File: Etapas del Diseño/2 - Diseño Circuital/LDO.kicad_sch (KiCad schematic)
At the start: 5 parts, among them Q1 2N3904, U1 TL431LP

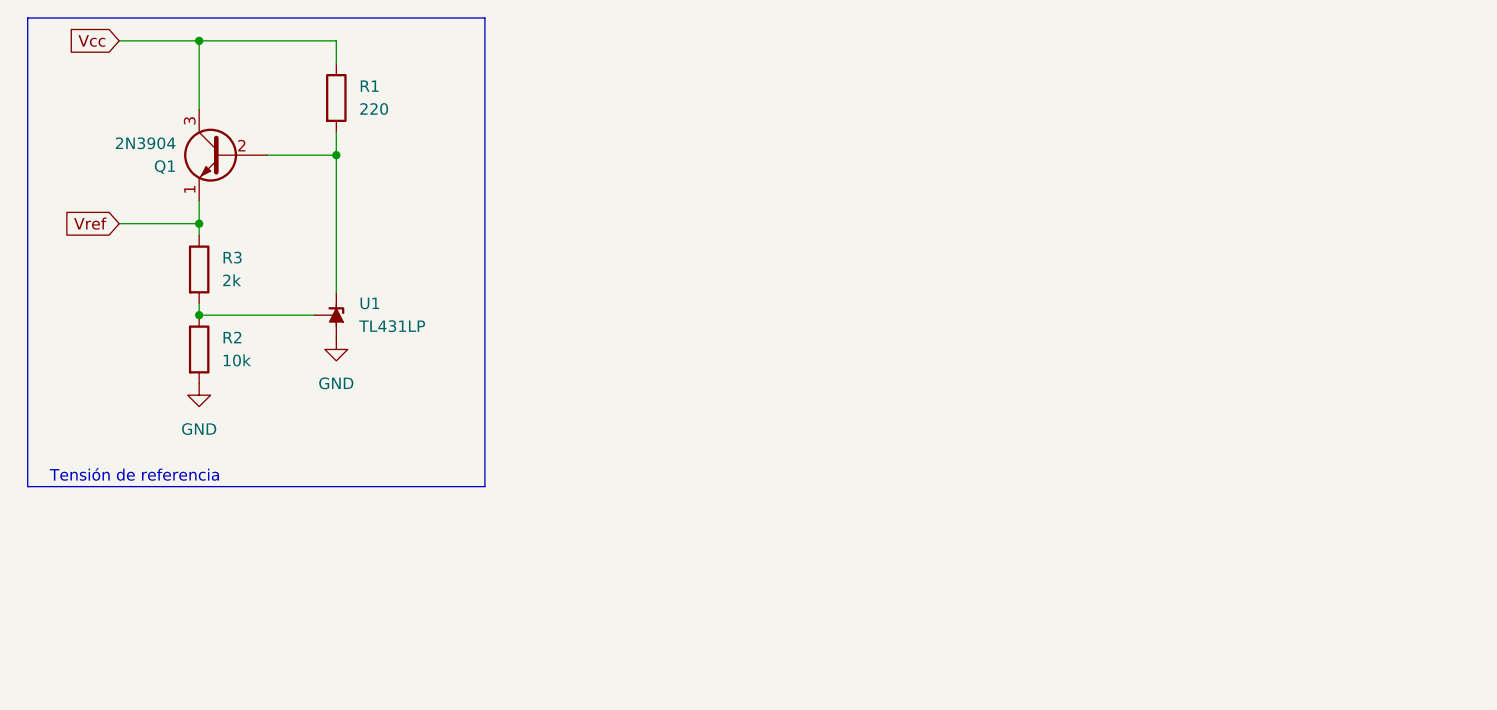
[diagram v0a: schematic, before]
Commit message: Vref y amplificador en esquemtico
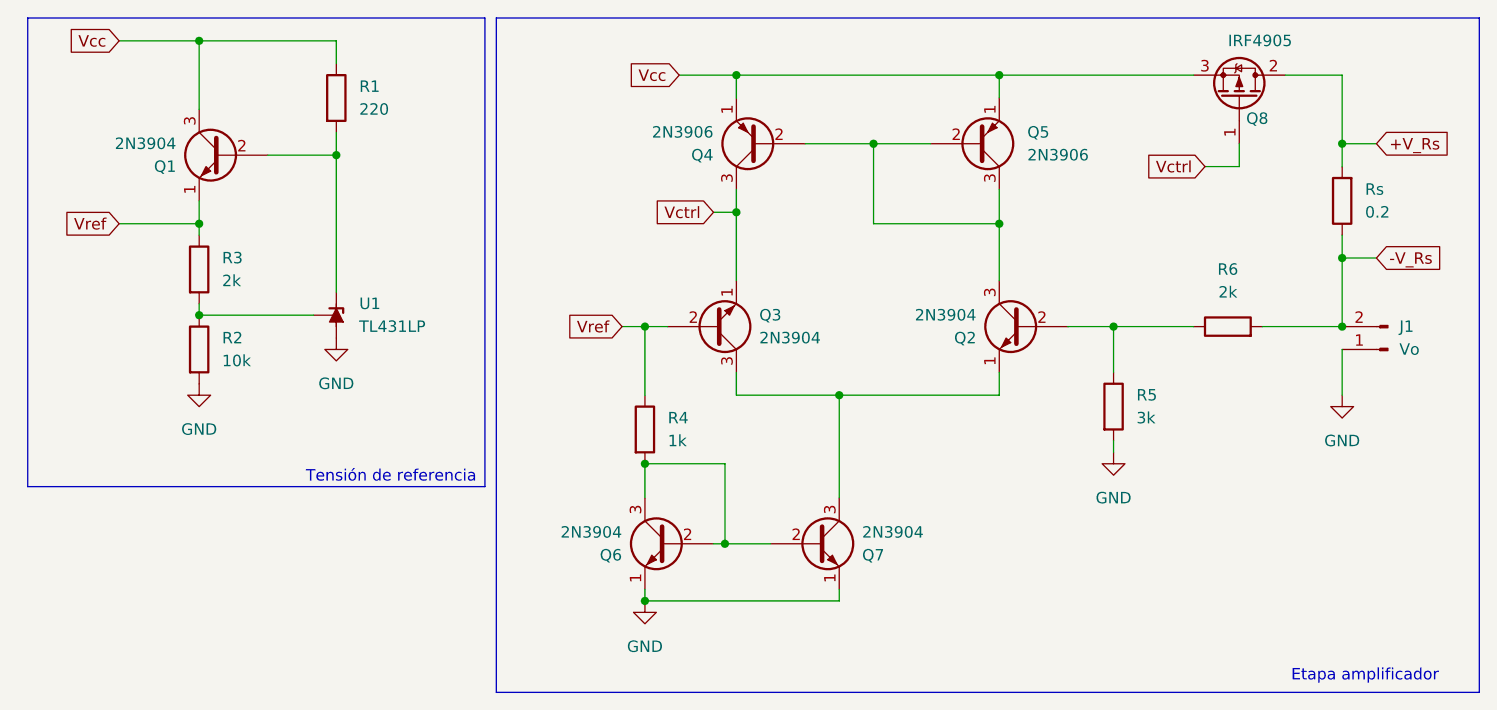
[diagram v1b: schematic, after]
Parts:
- added J1: Vo, symbol Connector:Conn_01x02_Pin
- added Q2, Q3, Q6, Q7: 2N3904, Package_TO_SOT_THT:TO-92_Inline, symbol Transistor_BJT:2N3904
- added Q4, Q5: 2N3906, Package_TO_SOT_THT:TO-92_Inline, symbol Transistor_BJT:2N3906
- added Q8: IRF4905, Package_TO_SOT_THT:TO-220-3_Vertical, symbol Transistor_FET:IRF4905
- added R4: 1k, symbol Device:R
- added R5: 3k, symbol Device:R
- added R6: 2k, symbol Device:R
- added Rs: 0.2, symbol Device:R
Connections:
- net GND: now also J1.1 (Pin_1), Q6.1 (E), Q7.1 (E), R5.2
- net Vcc: now also Q4.1 (E), Q5.1 (E), Q8.3 (S)
- net Vref: now also Q3.2 (B), R4.1
- new net: Q6.2 (B), Q6.3 (C), Q7.2 (B), R4.2
- new net: Q2.1 (E), Q3.3 (C), Q7.3 (C)
- new net: Q2.2 (B), R5.1, R6.1
- new net: Q2.3 (C), Q4.2 (B), Q5.2 (B), Q5.3 (C)
- new net +V_Rs: Q8.2 (D), Rs.2
- new net -V_Rs: J1.2 (Pin_2), R6.2, Rs.1
- new net Vctrl: Q3.1 (E), Q4.3 (C), Q8.1 (G)
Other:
- note added: "Etapa amplificador"

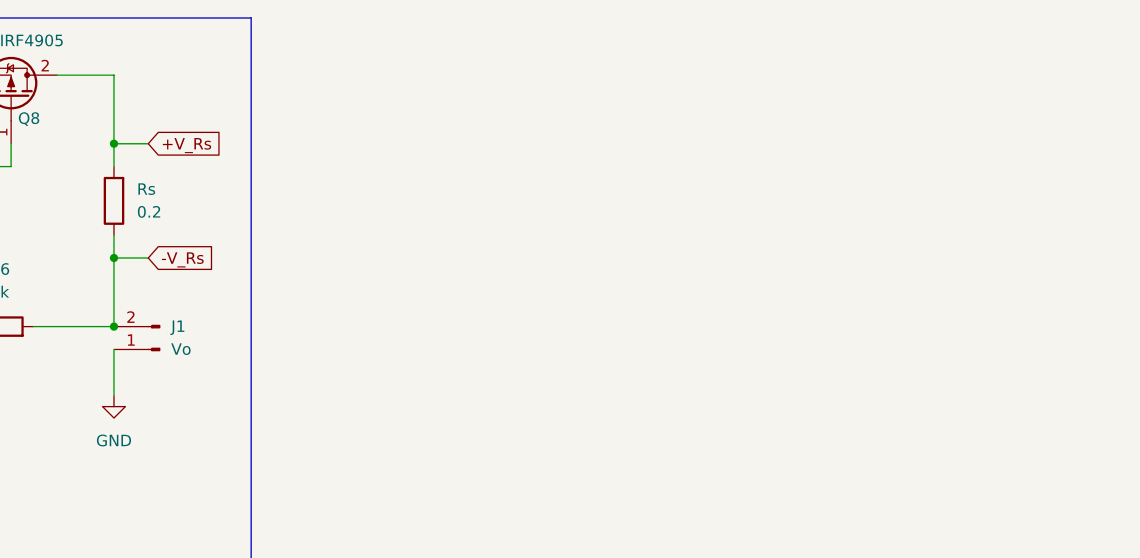
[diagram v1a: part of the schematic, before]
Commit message: Vref y amplificador en esquemtico 2
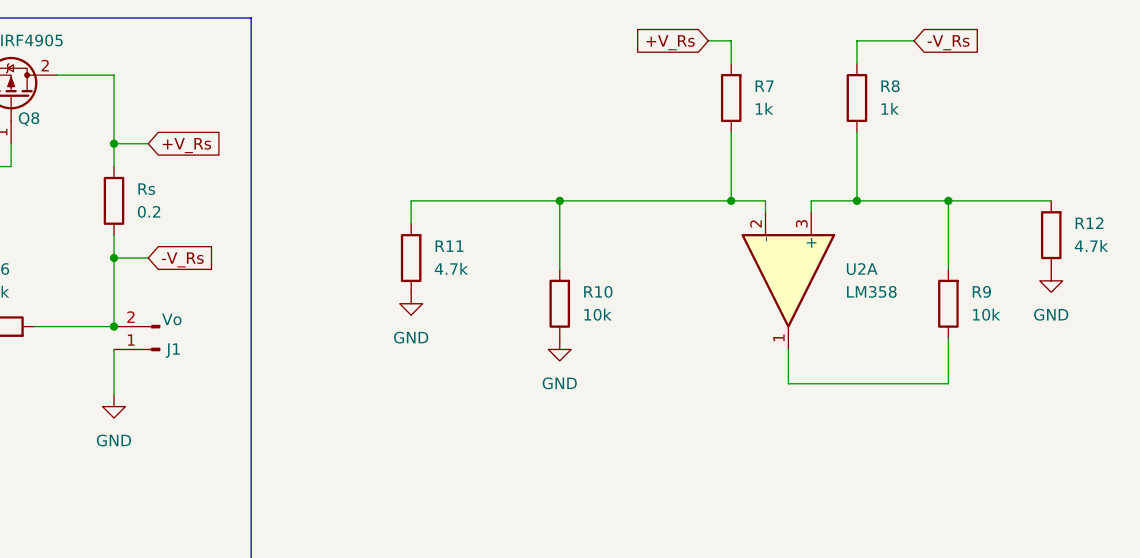
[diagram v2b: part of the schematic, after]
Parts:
- added R10, R9: 10k, symbol Device:R
- added R11, R12: 4.7k, symbol Device:R
- added R7, R8: 1k, symbol Device:R
- added U2: LM358, symbol Amplifier_Operational:LM358
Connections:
- net +V_Rs: now also R7.2
- net -V_Rs: now also R8.2
- net GND: now also R10.1, R11.1, R12.1
- new net: R9.1, U2.1
- new net: R10.2, R11.2, R7.1, U2.2 (-)
- new net: R12.2, R8.1, R9.2, U2.3 (+)

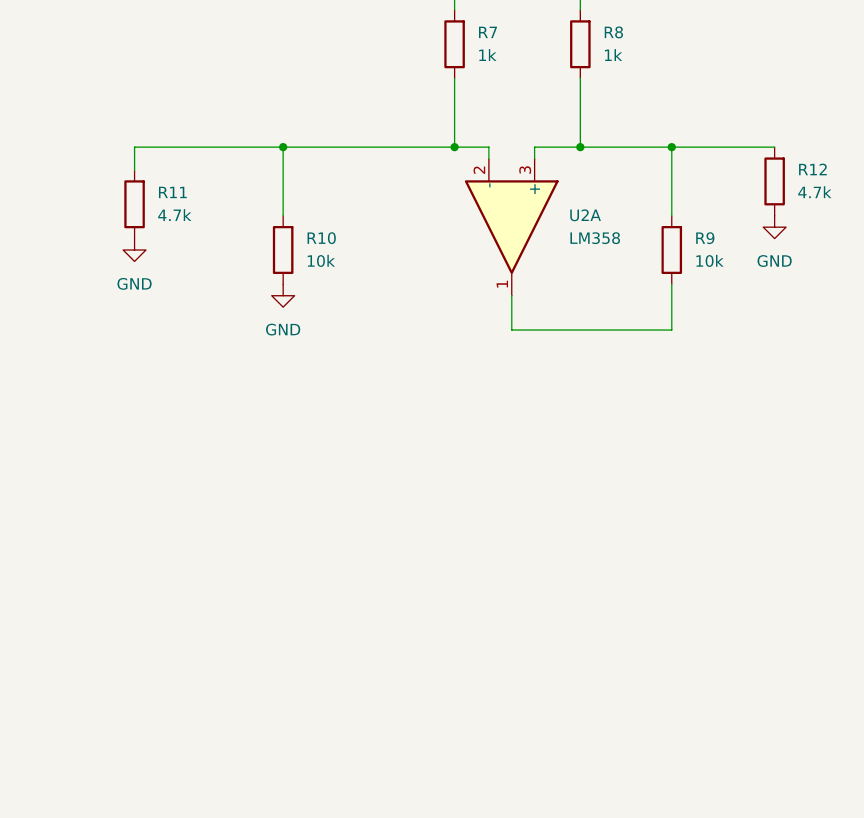
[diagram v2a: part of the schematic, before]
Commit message: Bloque aparte para el lazo de reg de corriente, tome referencias de Rs
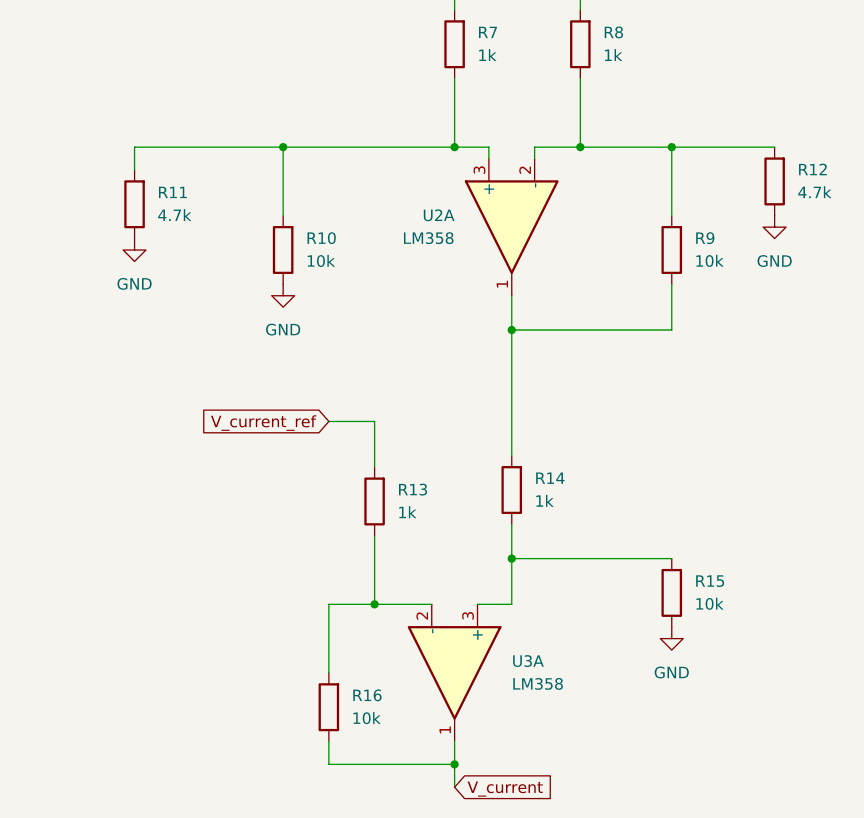
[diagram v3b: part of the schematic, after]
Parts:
- added R13, R14: 1k, symbol Device:R
- added R15, R16: 10k, symbol Device:R
- added U3: LM358, symbol Amplifier_Operational:LM358
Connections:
- net GND: now also R15.1
- net at R9.1, U2.1: now also R14.2
- net at R10.2, R11.2, R7.1: now also U2.3 (+); no longer U2.2 (-)
- net at R12.2, R8.1, R9.2: now also U2.2 (-); no longer U2.3 (+)
- new net: R14.1, R15.2, U3.3 (+)
- new net: R13.1, R16.2, U3.2 (-)
- new net V_current: R16.1, U3.1
- new net V_current_ref: R13.2
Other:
- moved on the sheet: U2A

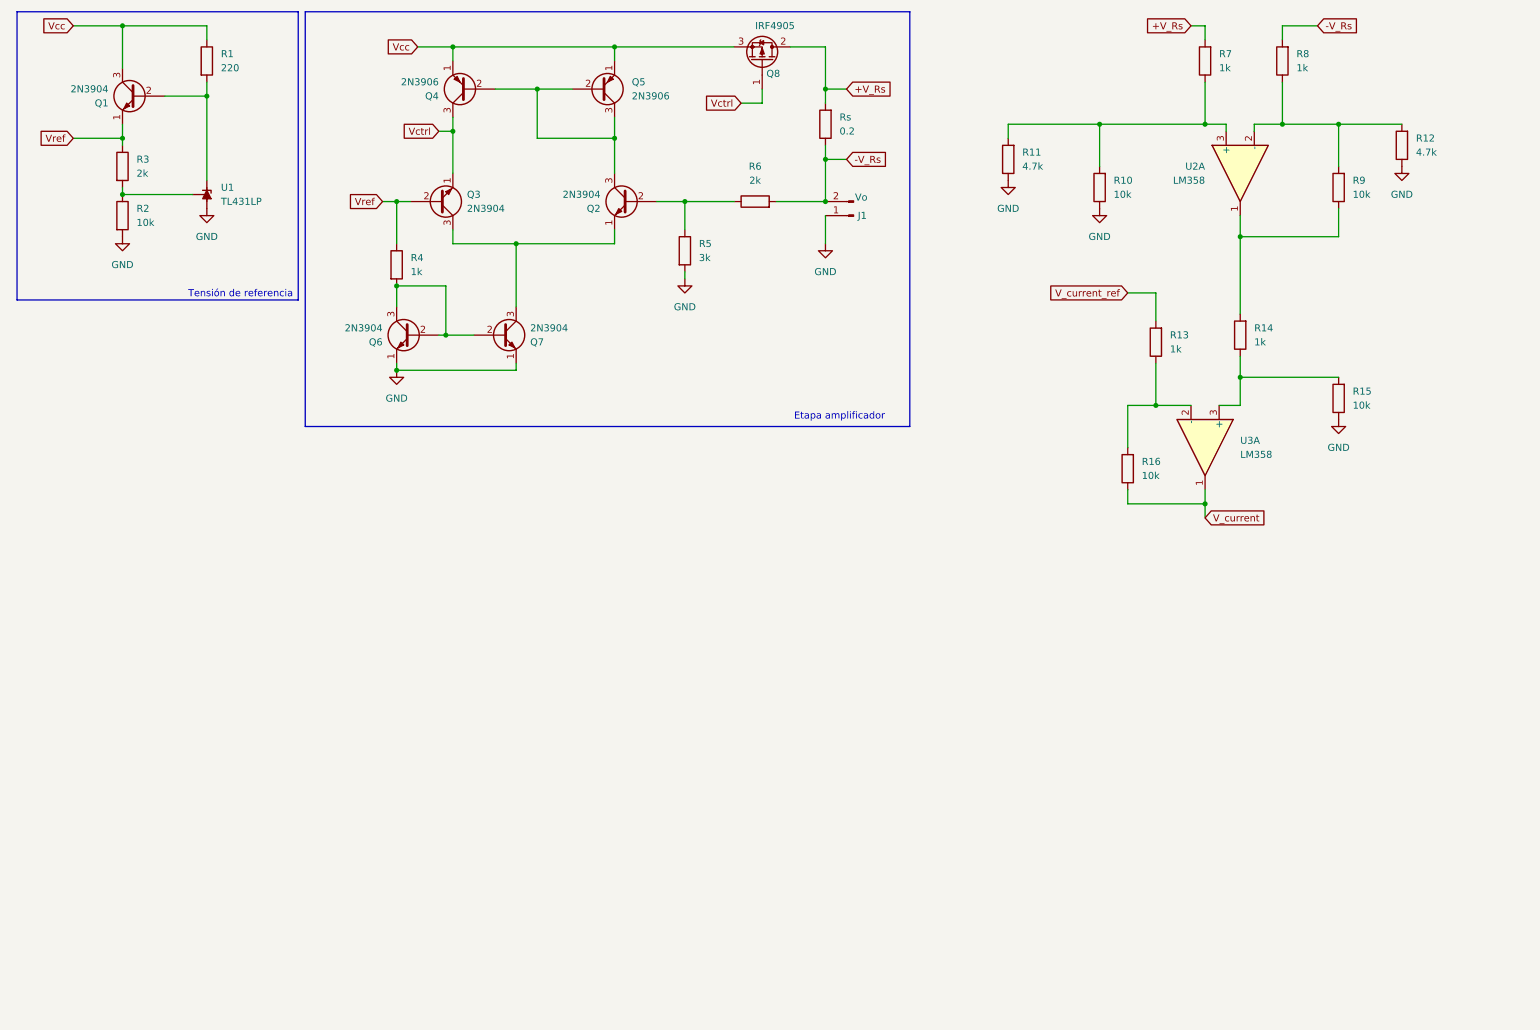
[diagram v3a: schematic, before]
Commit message: lazo de corriente y vref_current en esquematico
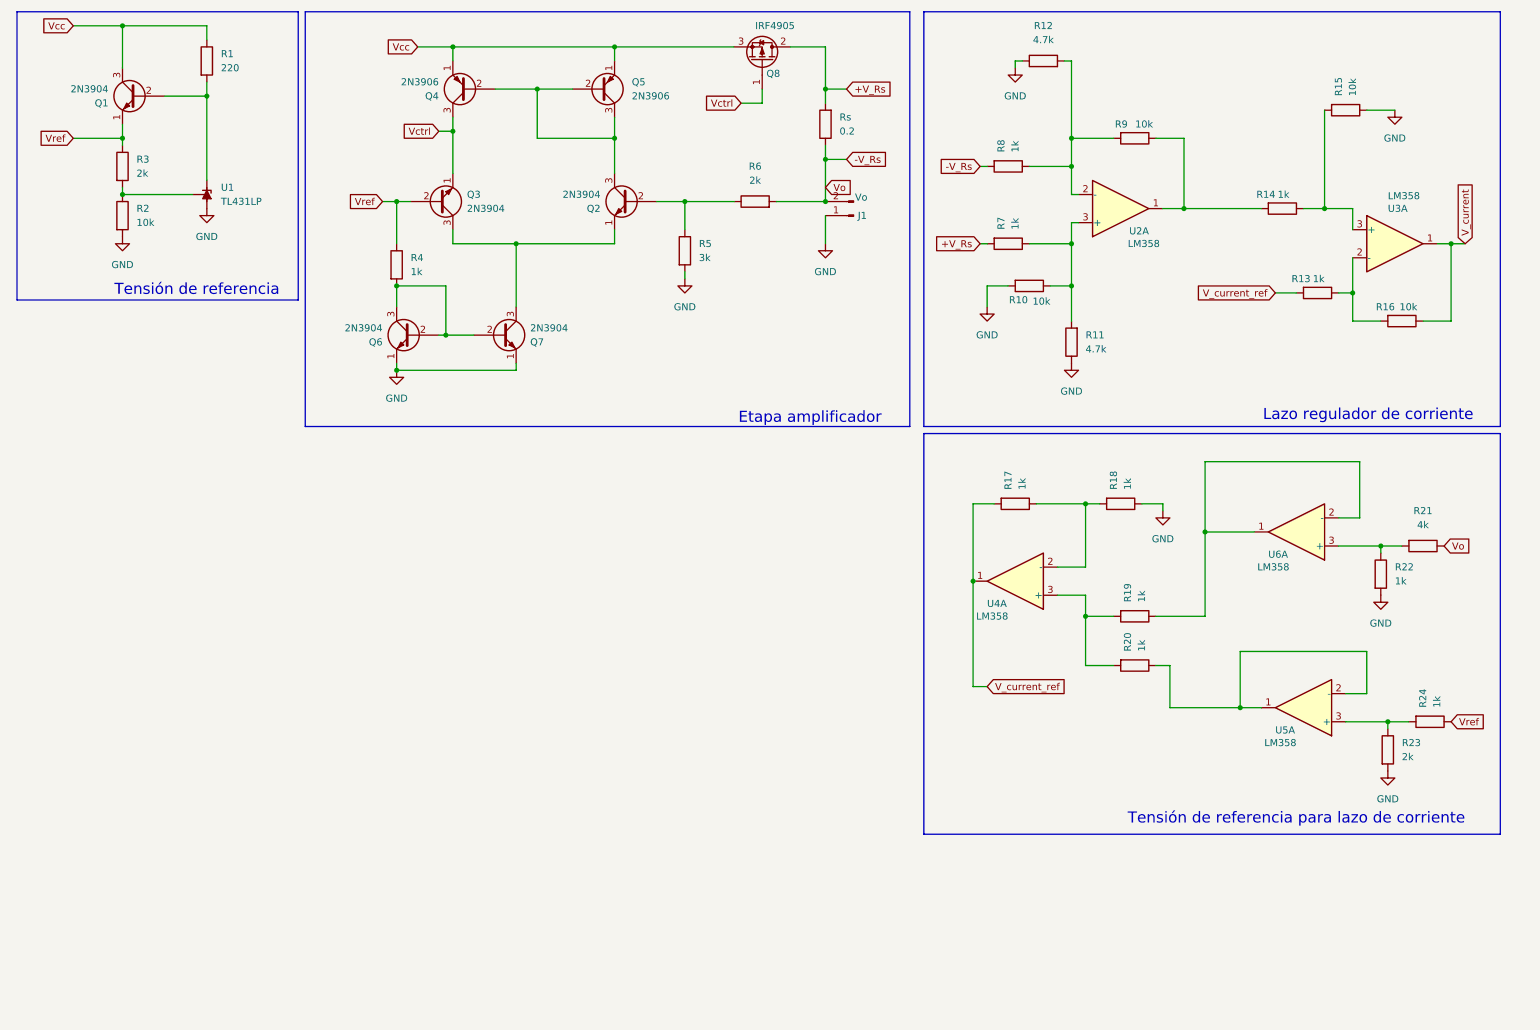
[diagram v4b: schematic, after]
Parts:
- added R17, R18, R19, R20, R22, R24: 1k, symbol Device:R
- added R21: 4k, symbol Device:R
- added R23: 2k, symbol Device:R
- added U4, U5, U6: LM358, symbol Amplifier_Operational:LM358
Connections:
- net -V_Rs: now also R21.1
- net GND: now also R10.2, R18.1, R22.2, R23.2; no longer R10.1
- net V_current_ref: now also R17.2, U4.1
- net Vref: now also R24.1
- net at R11.2, R7.1, U2.3 (+): now also R10.1; no longer R10.2
- new net: R19.1, U6.1, U6.2 (-)
- new net: R21.2, R22.1, U6.3 (+)
- new net: R23.1, R24.2, U5.3 (+)
- new net: R20.1, U5.1, U5.2 (-)
- new net: R19.2, R20.2, U4.3 (+)
- new net: R17.1, R18.2, U4.2 (-)
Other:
- note added: "Lazo regulador de corriente"
- note added: "Tensión de referencia para lazo de corriente"
- moved on the sheet: R10, R11, R12, R13, R14, R15, R16, R7, R8, R9, U2A, U3A
